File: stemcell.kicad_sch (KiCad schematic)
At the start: 36 parts, among them J1 USB C Connector, J2 Left, J3 Right, J4 Down, SW1 Boot0, U1 STM32F4x1CxUx, U2 XC6220B331MR, Y1 HSE1 8Mhz 12pF

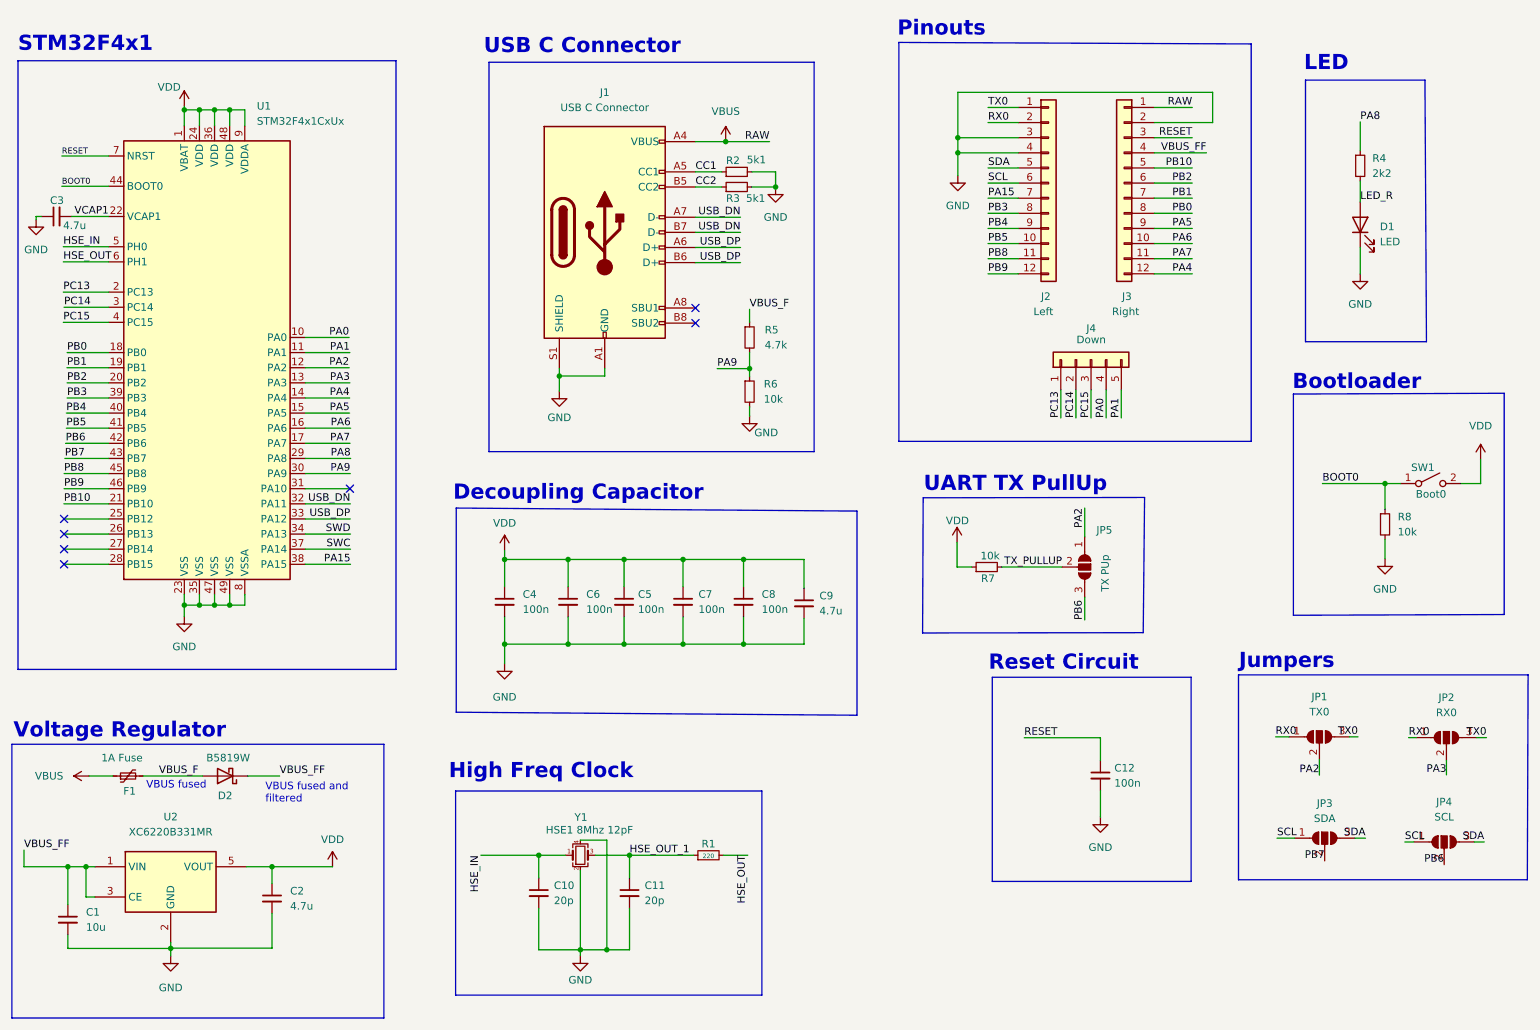
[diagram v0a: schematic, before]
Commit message: Rerouted USB section to fit replacement USB connector PN C2874573
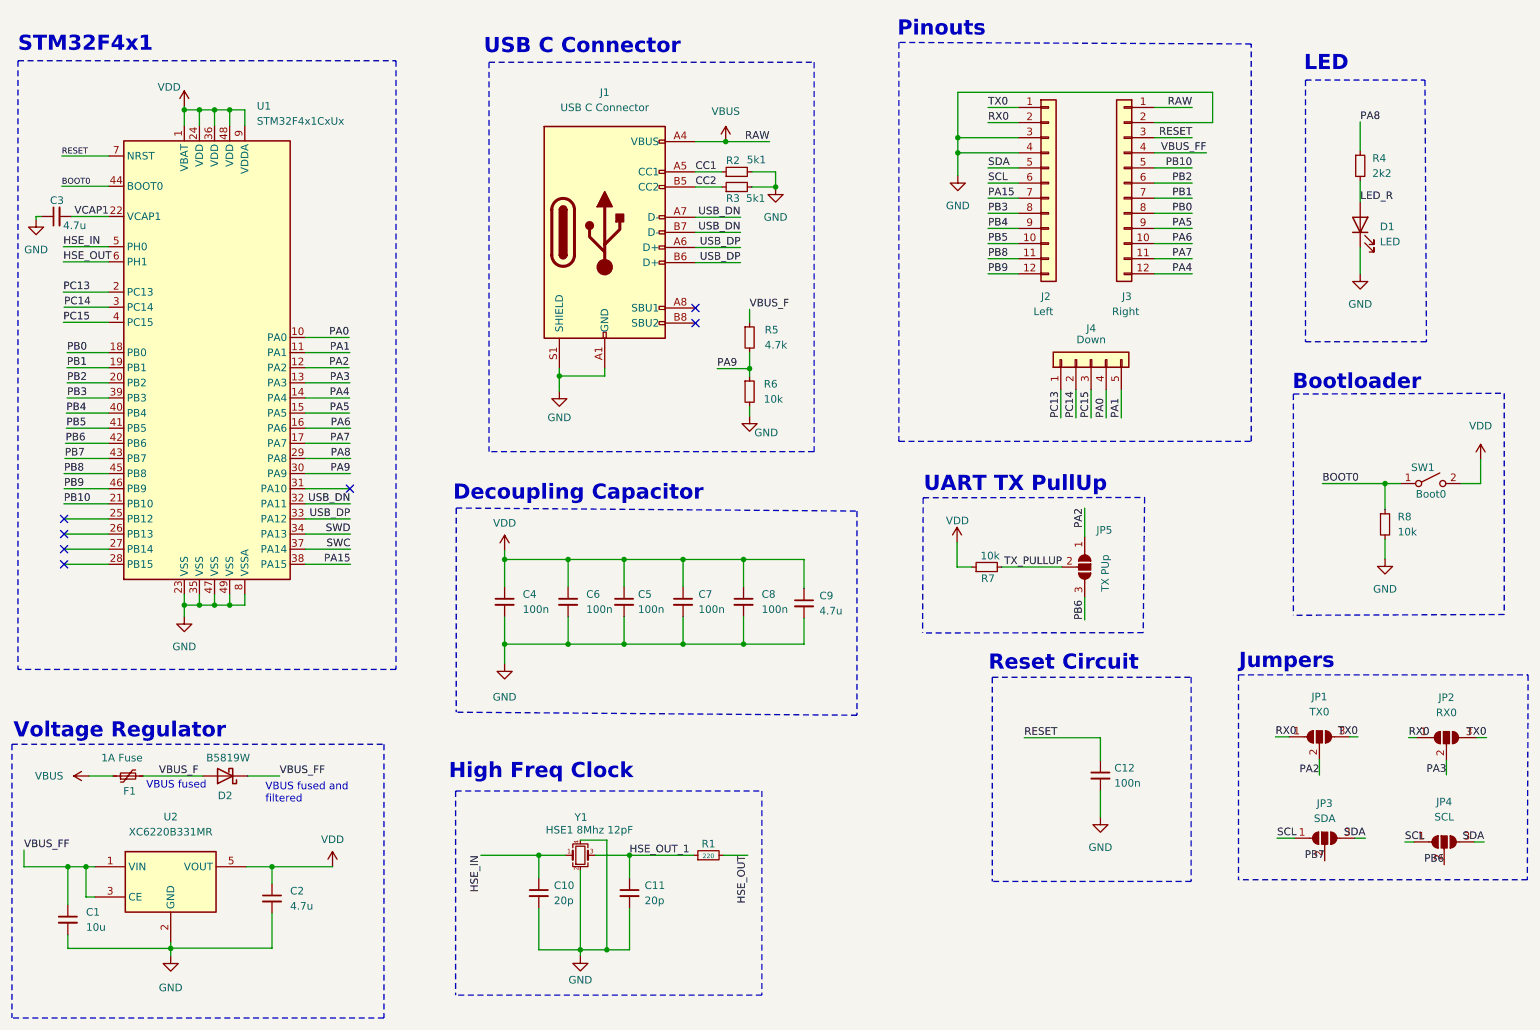
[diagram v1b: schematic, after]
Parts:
- J1: footprint stemcell:USB-C-C168688 -> stemcell:USB-C-SMD_MC-109-C10; LCSC C2681554 -> C2874573
